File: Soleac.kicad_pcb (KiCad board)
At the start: 2 copper layers, 32 parts, among them J1 Regulador de voltaje, J2 Sensor MQ-2, SW1 SW_SPST, U1 LM358, U2 LM358, U3 ESP32-DEVKITC-32D, U4 ER_OLEDM0.91_1x-I2C

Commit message: conexiones en el PCB
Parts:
- BZ2: moved to B.Cu
- moved R14 293.0 mm to (312.0, 107.9)
- moved R15 293.0 mm to (312.0, 112.6)
- moved R11 281.1 mm to (309.9, 126.5), turned to 180 degrees
- moved Murata1 222.8 mm to (347.8, 181.2)
- moved J2 203.1 mm to (324.8, 176.2), turned to -90 degrees
- moved R1 178.7 mm to (329.7, 150.6), turned to 180 degrees
- moved C2 158.7 mm to (308.8, 150.7), turned to 180 degrees
- moved C1 156.4 mm to (316.9, 160.2), turned to 180 degrees
- moved R5 152.9 mm to (322.1, 169.7), turned to 180 degrees
- moved R2 148.7 mm to (309.0, 160.2), turned to 180 degrees
- moved U4 137.5 mm to (201.3, 191.2), turned to -90 degrees
- moved C3 131.5 mm to (301.4, 169.7), turned to 0 degrees
- moved R3 126.8 mm to (315.1, 191.5), turned to 90 degrees
- moved R4 125.7 mm to (309.6, 184.8), turned to -90 degrees
- moved C5 123.1 mm to (292.5, 173.2)
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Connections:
- D2 pad 1: Net-(D2-K) -> Earth
- D2 pad 2: /GPIO26 (LED) -> Net-(D2-A)
- R11 pad 1: Earth -> Net-(D2-A)
- R11 pad 2: Net-(D2-K) -> /GPIO26 (LED)
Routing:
- net /GPIO26 (LED): track 0.00 -> 78.5 mm
- net /GPIO25 (BUZZER): track 0.00 -> 73.7 mm
- net Net-(U3-IO34): track 90.2 -> 41.9 mm
- net Earth: track 154.8 -> 202.2 mm
- net /5V: track 0.00 -> 7.65 mm
- net /GPIO27 (CLOCK): track 0.00 -> 7.16 mm, vias 0 -> 1
- net /GPIO14 (DATA): track 0.00 -> 7.12 mm, vias 0 -> 1
- net Net-(U2A-+): track 12.5 -> 6.97 mm
- net Net-(D2-A): track 0.00 -> 4.38 mm
- net Net-(C5-Pad1): track 9.64 -> 6.40 mm
- net Net-(R10-Pad1): track 13.6 -> 16.8 mm
- net Net-(C2-Pad2): track 25.5 -> 28.2 mm
- net Net-(U2A--): track 20.8 -> 19.1 mm
- net Net-(U1A--): track 20.6 -> 19.8 mm
- net Net-(U1A-+): track 26.6 -> 27.2 mm

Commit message: Conexión Completa
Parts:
- removed MK1: SPH0641LU4H-1, Sensor_Audio:Knowles_LGA-5_3.5x2.65mm
- removed Murata1: MA40S4R, Connector:FanPinHeader_1x04_P2.54mm_Vertical
- moved R14 91.6 mm to (319.5, 199.2), turned to 90 degrees
- moved SW1 81.2 mm to (215.0, 179.6), turned to 90 degrees
- moved R15 79.9 mm to (311.0, 192.5), turned to -90 degrees
- moved J1 47.6 mm to (215.0, 155.2), turned to 90 degrees
- moved BT1 37.9 mm to (186.6, 142.8), turned to 90 degrees
- moved BZ2 9.19 mm to (300.7, 136.0)
- moved C1 7.74 mm to (311.5, 154.6), turned to -90 degrees
- moved R1 7.50 mm to (322.9, 147.5)
- moved J2 6.17 mm to (319.5, 173.1)
- moved C2 5.09 mm to (304.8, 147.5)
- moved C3 5.09 mm to (297.4, 166.5)
- moved C4 5.09 mm to (279.6, 173.5)
- moved C5 5.09 mm to (288.5, 170.1)
- moved D2 5.09 mm to (312.8, 123.3)
- moved R10 5.09 mm to (278.5, 197.5)
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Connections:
- U4 pad 2: /3.3V -> /5V
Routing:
- net /5V: track 7.65 -> 241.2 mm
- net Earth: track 202.2 -> 412.9 mm
- net Net-(J2-Pin_3): track 0.00 -> 13.6 mm
- net /GPIO35 (MQ-2): track 0.00 -> 11.0 mm
- net /GPIO22 (SCL OLED): track 0.00 -> 7.97 mm
- net /GPIO23 (SDA OLED): track 0.00 -> 7.61 mm
- net Net-(Murata1-A): track 0.00 -> 5.85 mm, vias 0 -> 1
- net Net-(C1-Pad1): track 17.7 -> 13.1 mm
- net /GPIO25 (BUZZER): track 73.7 -> 69.4 mm
- net /GPIO26 (LED): track 78.5 -> 75.8 mm
- net Net-(U3-IO34): track 41.9 -> 39.2 mm
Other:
- board text added: "MEMS"
- board text added: "MURATA"

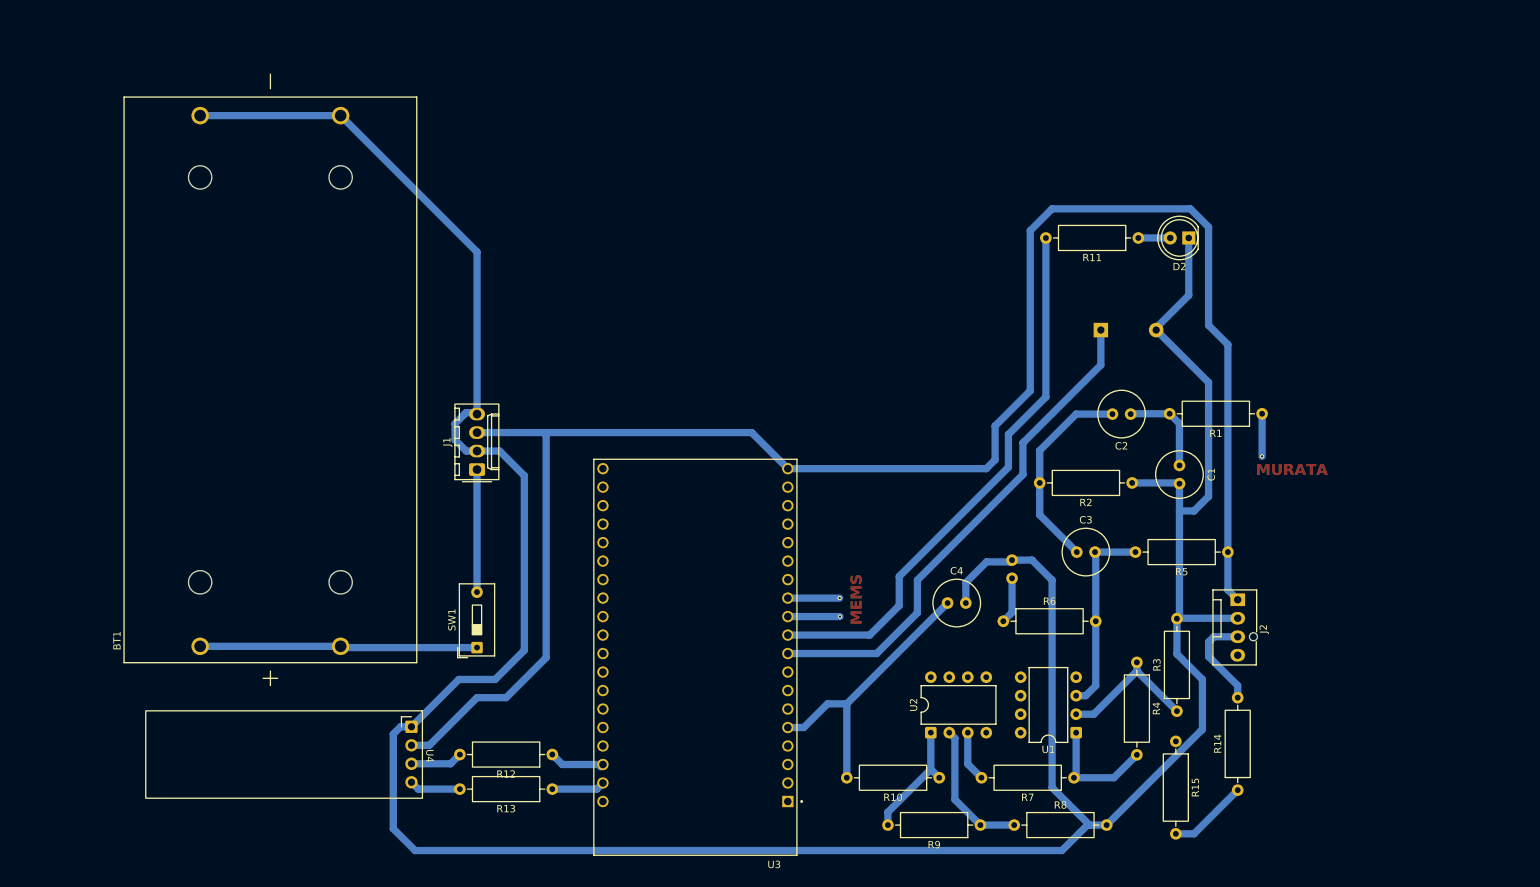
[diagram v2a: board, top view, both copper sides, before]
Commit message: Separación de PCBs
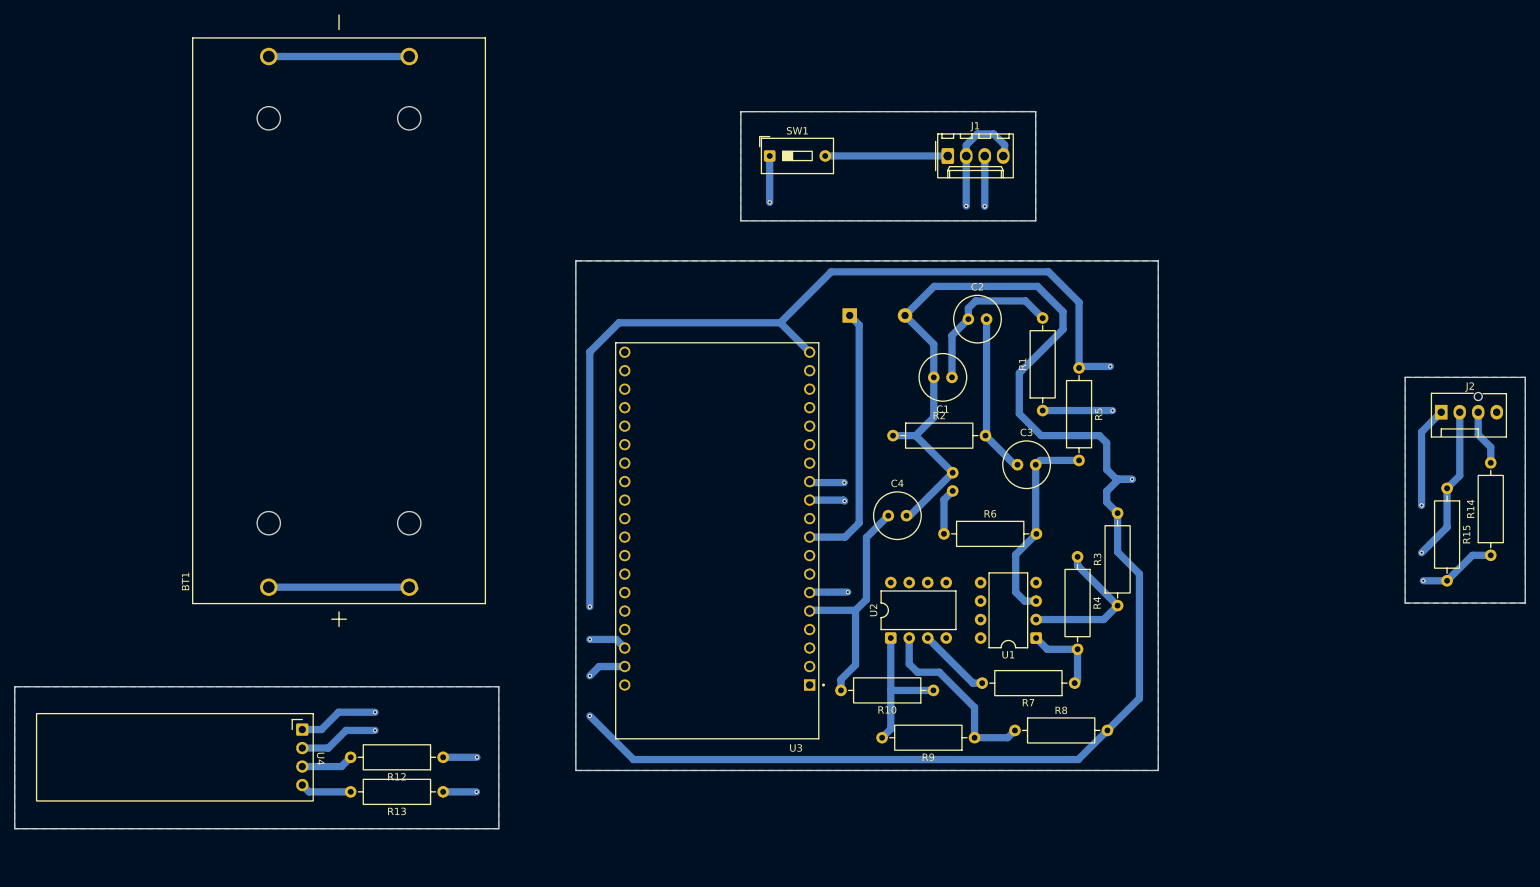
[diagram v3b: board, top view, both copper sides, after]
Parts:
- removed D2: LED, LED_THT:LED_D5.0mm
- removed R11: R, Resistor_THT:R_Axial_DIN0309_L9.0mm_D3.2mm_P12.70mm_Horizontal
- moved SW1 78.6 mm to (255.2, 112.1), turned to 0 degrees
- moved J1 77.7 mm to (279.7, 112.1), turned to 0 degrees
- moved R15 51.0 mm to (348.3, 157.7)
- moved R14 47.4 mm to (354.3, 166.9)
- moved J2 38.0 mm to (347.5, 147.3), turned to 0 degrees
- moved BZ2 34.6 mm to (266.2, 134.0)
- moved C1 33.5 mm to (280.2, 142.5), turned to 180 degrees
- moved R2 33.5 mm to (272.1, 150.5), turned to 0 degrees
- moved R5 32.5 mm to (297.7, 141.2), turned to -90 degrees
- moved R1 30.1 mm to (292.7, 147.1), turned to 90 degrees
- moved C2 25.8 mm to (282.5, 134.5), turned to 0 degrees
- moved R3 16.6 mm to (303.0, 173.8)
- moved R4 16.6 mm to (297.5, 167.2)
- moved U3 16.3 mm to (248.0, 165.0)
- moved R12 15.0 mm to (210.3, 194.7)
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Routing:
- net Earth: track 412.9 -> 285.1 mm, vias 0 -> 5
- net /5V: track 241.2 -> 159.4 mm, vias 0 -> 5
- net /GPIO26 (LED): track 75.8 -> 0.00 mm
- net /GPIO25 (BUZZER): track 69.4 -> 36.6 mm
- net Net-(SW1-A): track 38.1 -> 26.6 mm, vias 0 -> 1
- net Net-(C1-Pad1): track 13.1 -> 22.0 mm
- net Net-(U3-IO34): track 39.2 -> 33.0 mm
- net Net-(C2-Pad2): track 28.2 -> 22.1 mm
- net Net-(U2A--): track 19.1 -> 25.1 mm
- net Net-(J2-Pin_3): track 13.6 -> 7.66 mm
- net Net-(R4-Pad2): track 16.3 -> 11.1 mm
- net /GPIO35 (MQ-2): track 11.0 -> 16.0 mm, vias 0 -> 2
- net Net-(D2-A): track 4.38 -> 0.00 mm
- net Net-(Murata1-A): track 5.85 -> 9.61 mm
- net Net-(R10-Pad1): track 16.8 -> 20.0 mm
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- added copper zone on B.Cu, net (none)
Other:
- board outline added: 207.5 x 98.5 mm
- board text added: "DISPLAY"
- board text added: "MQ - 2"

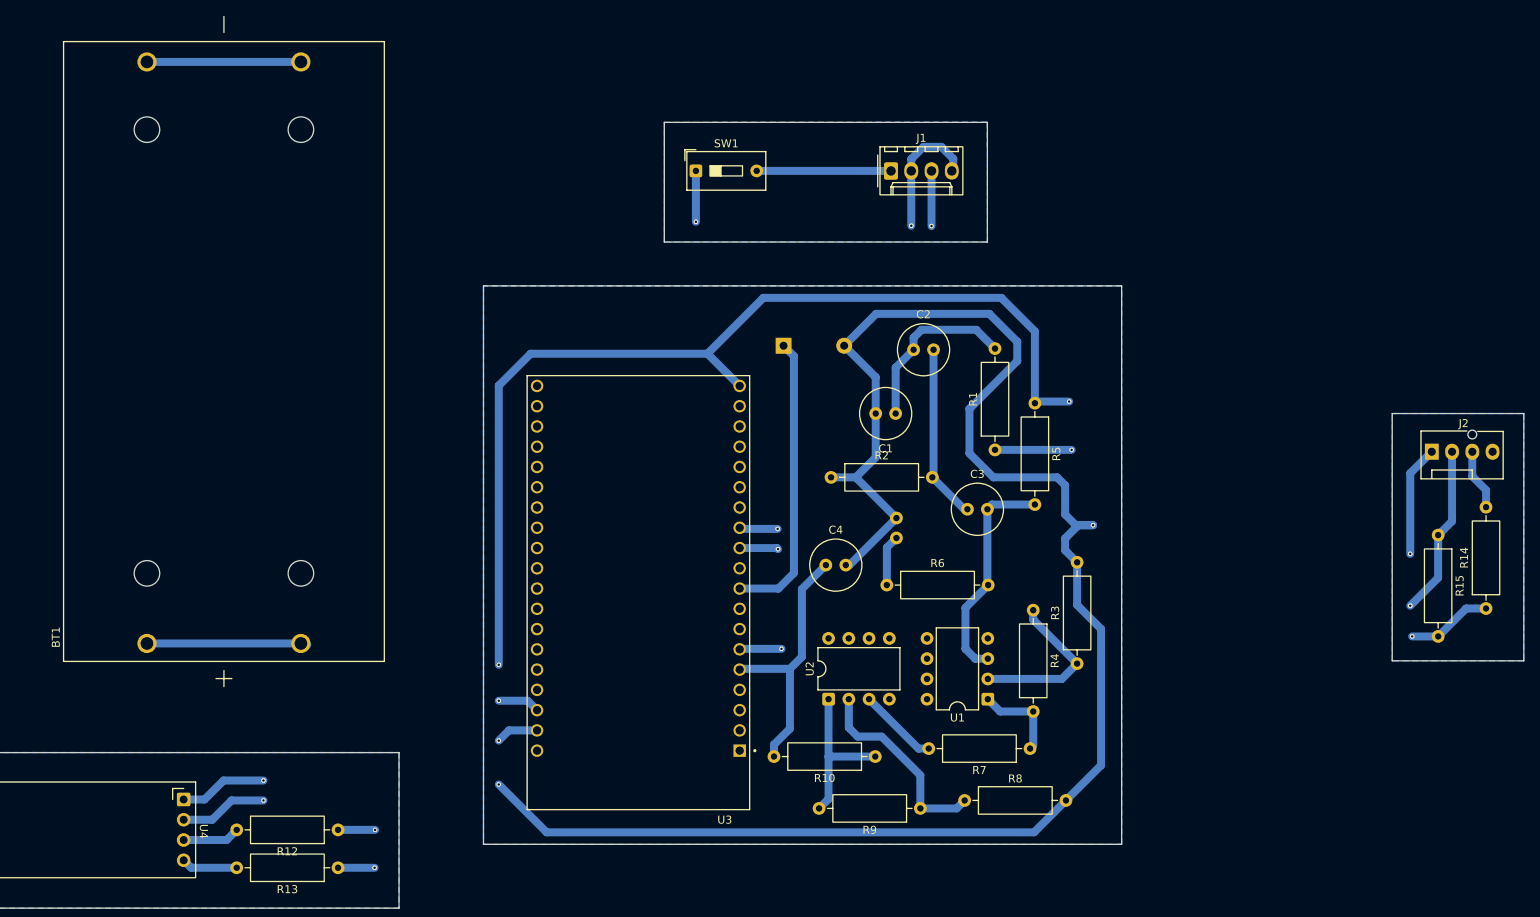
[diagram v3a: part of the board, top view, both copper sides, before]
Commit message: Conexión entre placas
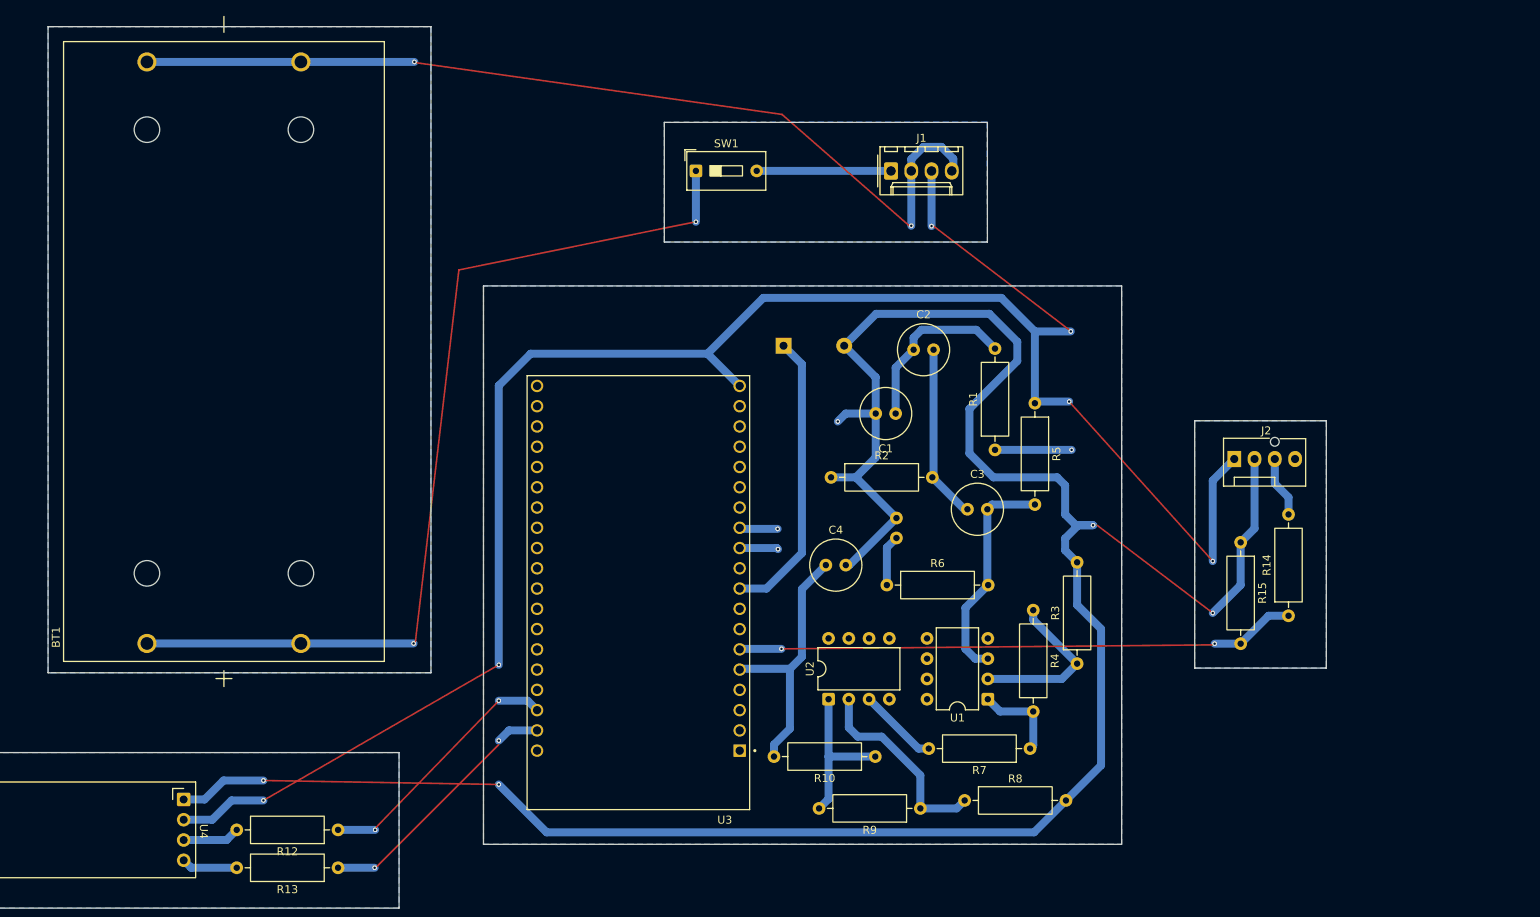
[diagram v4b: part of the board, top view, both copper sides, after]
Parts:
- moved J2 24.8 mm to (322.7, 148.2)
- moved R14 24.8 mm to (329.5, 167.8)
- moved R15 24.8 mm to (323.5, 158.7)
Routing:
- net Earth: track 285.1 -> 304.5 mm, vias 5 -> 7
- net Net-(SW1-A): track 26.6 -> 40.7 mm, vias 1 -> 2
- net /5V: track 159.4 -> 163.9 mm, vias 5 -> 6
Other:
- board size 207.5 x 98.5 mm -> 182.7 x 110.5 mm
